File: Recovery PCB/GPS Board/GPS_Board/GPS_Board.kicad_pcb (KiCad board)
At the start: 2 copper layers, 85.7 x 50.8 mm, 9 parts, among them J1 XT30-M, J2 XT30-M, U1 Teensy4.1, U2 D24V22F5_VoltageRegulator, U3 LD1117v33

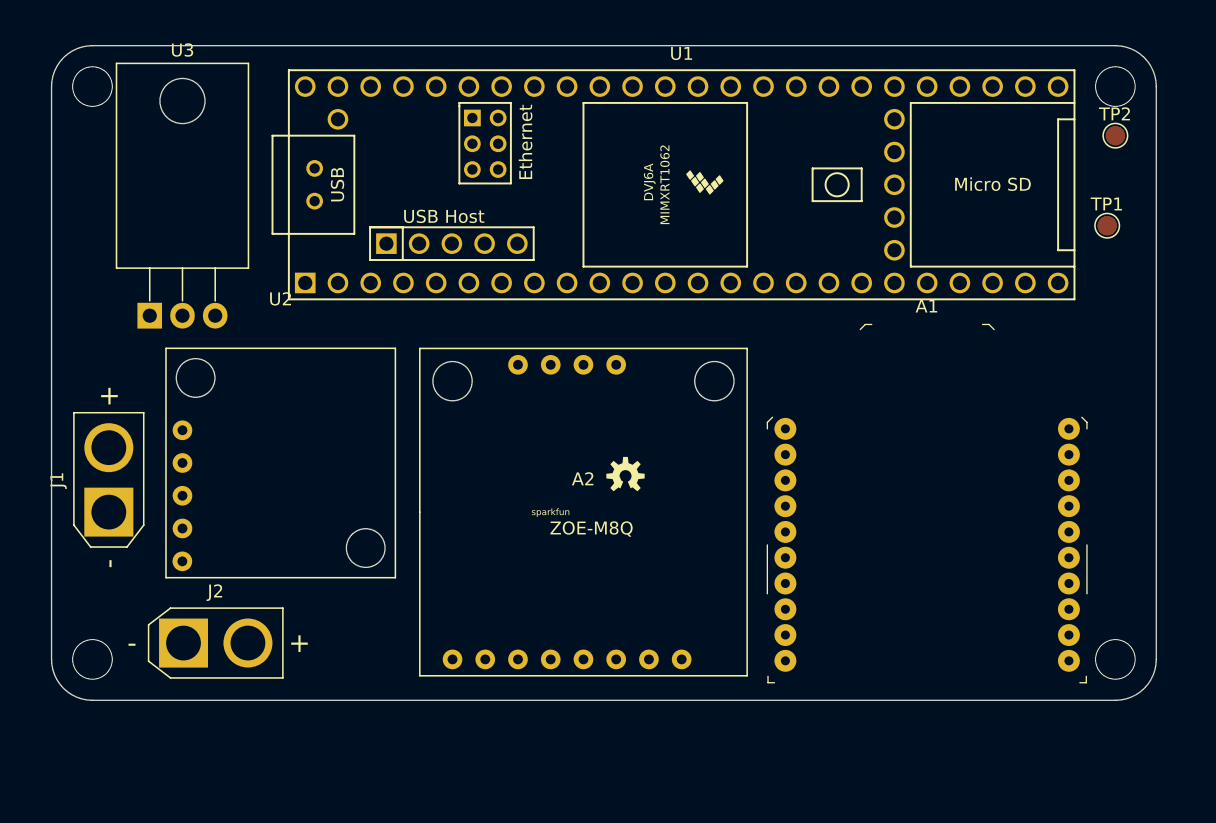
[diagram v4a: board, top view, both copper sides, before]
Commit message: Power Traces Outline
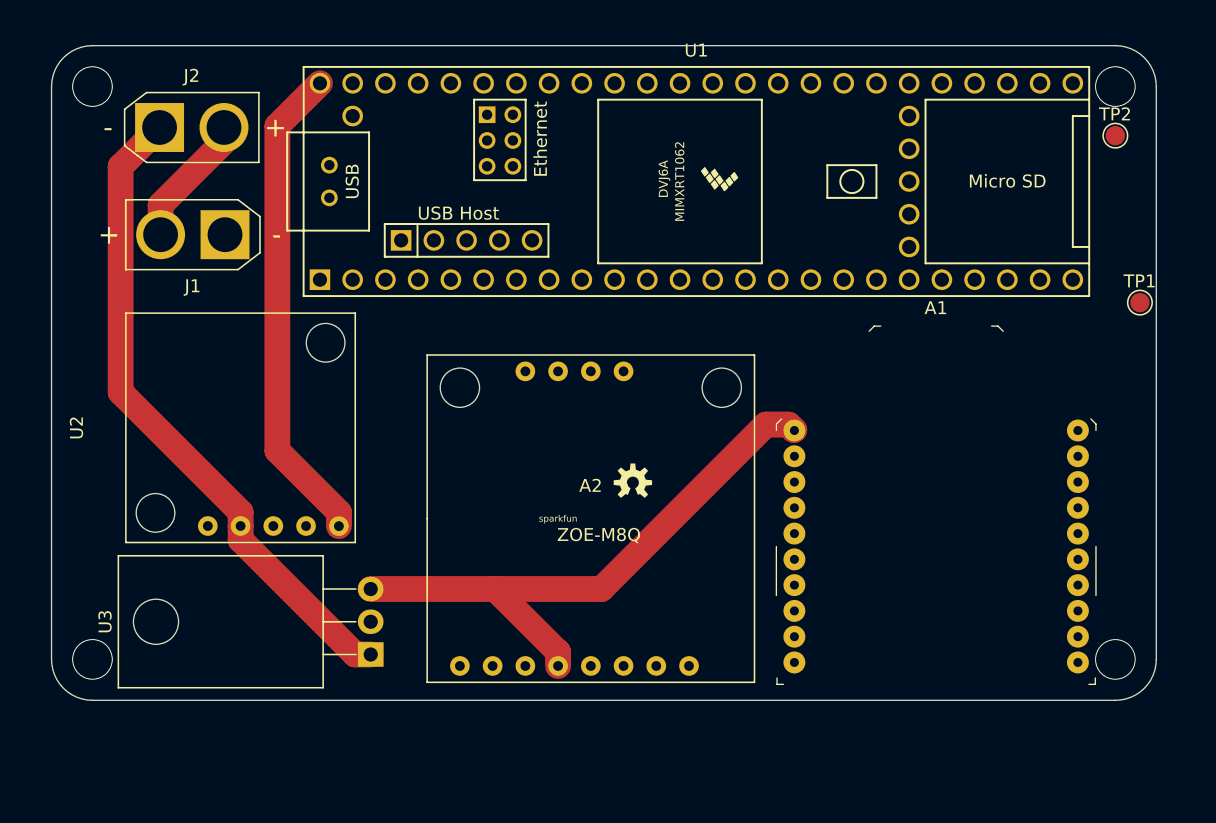
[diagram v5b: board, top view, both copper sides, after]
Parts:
- moved J2 40.0 mm to (119.5, 66.7)
- moved U3 31.4 mm to (135.9, 107.6), turned to 90 degrees
- moved J1 23.3 mm to (124.6, 75.0), turned to 180 degrees
- moved TP1 6.49 mm to (195.6, 80.3)
- moved U2 4.14 mm to (125.8, 90.0), turned to 90 degrees
- moved U1 1.17 mm to (161.2, 70.9)
- moved A2 0.76 mm to (153.0, 97.0)
- moved A1 0.71 mm to (179.8, 99.2)
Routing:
- net Net-(J2-Pad1): track 0.00 -> 50.9 mm
- net +3V3: track 0.00 -> 46.3 mm
- net +5V: track 0.00 -> 37.7 mm
- net Net-(J1-Pad2): track 0.00 -> 10.4 mm
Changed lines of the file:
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@@
     (thickness 1.6)
     (drawings 8)
-    (tracks 4)
+    (tracks 26)
     (zones 0)
     (modules 9)
@@
   )
   (setup
-    (last_trace_width 0.25)
+    (last_trace_width 2)
     (user_trace_width 0.25)
     (user_trace_width 0.4)
@@
   )
   (module "GPS Board:XBEE-20_THT" (layer F.Cu)
-    (at 179.07 99.06)
+    (at 179.7685 99.187)
     (descr https://www.digi.com/pdf/ds_xbeemultipointmodules.pdf)
     (fp_text reference A1 (at 0 -18.49) (layer F.SilkS)
@@
   )
   (module "GPS Board:Sparkfun-GPS-ZOE-M8Q-Breakout" (layer F.Cu)
-    (at 152.4 96.52)
+    (at 152.9715 97.028)
     (fp_text reference A2 (at 0 -2.54) (layer F.SilkS)
       (effects (font (size 1 1) (thickness 0.15)))
@@
   )
   (module Connector_AMASS:AMASS_XT30U-M_1x02_P5.0mm_Vertical (layer F.Cu)
-    (at 115.57 96.52 90)
+    (at 124.587 74.9935 180)
     (descr "Connector XT30 Vertical Cable Male, https://www.tme.eu/en/Document/3cbfa5cfa544d79584972dd5234a409e/XT30U%20SPEC.pdf")
     (tags "RC Connector XT30")
-    (fp_text reference J1 (at 2.5 -4 90) (layer F.SilkS)
-      (effects (font (size 1 1) (thickness 0.15)))
-    )
-    (fp_text value XT30-M (at 2.5 4 90) (layer F.Fab)
+    (fp_text reference J1 (at 2.5 -4) (layer F.SilkS)
+      (effects (font (size 1 1) (thickness 0.15)))
+    )
+    (fp_text value XT30-M (at 2.5 4) (layer F.Fab)
       (effects (font (size 1 1) (thickness 0.15)))
     )
@@
     (fp_line (start 7.6 -2.6) (end 7.6 2.6) (layer F.Fab) (width 0.1))
     (fp_line (start -2.6 -1.3) (end -2.6 1.3) (layer F.Fab) (width 0.1))
-    (fp_text user %R (at 2.5 0 90) (layer F.Fab)
-      (effects (font (size 1 1) (thickness 0.15)))
-    )
-    (fp_text user + (at 9 0 90) (layer F.SilkS)
+    (fp_text user %R (at 2.5 0) (layer F.Fab)
+      (effects (font (size 1 1) (thickness 0.15)))
+    )
+    (fp_text user + (at 9 0) (layer F.SilkS)
       (effects (font (size 1.5 1.5) (thickness 0.15)))
     )
-    (fp_text user - (at -4 0 90) (layer F.SilkS)
+    (fp_text user - (at -4 0) (layer F.SilkS)
       (effects (font (size 1.5 1.5) (thickness 0.15)))
     )
-    (pad 1 thru_hole rect (at 0 0 90) (size 3.8 3.8) (drill 2.7) (layers *.Cu *.Mask)
-      (net 1 GND))
-    (pad 2 thru_hole circle (at 5 0 90) (size 3.8 3.8) (drill 2.7) (layers *.Cu *.Mask)
+    (pad 1 thru_hole rect (at 0 0 180) (size 3.8 3.8) (drill 2.7) (layers *.Cu *.Mask)
+      (net 1 GND))
+    (pad 2 thru_hole circle (at 5 0 180) (size 3.8 3.8) (drill 2.7) (layers *.Cu *.Mask)
       (net 3 "Net-(J1-Pad2)"))
     (model ${KISYS3DMOD}/Connector_AMASS.3dshapes/AMASS_XT30U-M_1x02_P5.0mm_Vertical.wrl
@@
   )
   (module Connector_AMASS:AMASS_XT30U-M_1x02_P5.0mm_Vertical (layer F.Cu)
-    (at 121.365 106.68)
+    (at 119.507 66.675)
     (descr "Connector XT30 Vertical Cable Male, https://www.tme.eu/en/Document/3cbfa5cfa544d79584972dd5234a409e/XT30U%20SPEC.pdf")
     (tags "RC Connector XT30")
@@
   )
   (module TestPoint:TestPoint_Pad_D1.5mm (layer F.Cu)
-    (at 193.04 74.295)
+    (at 195.58 80.264)
     (descr "SMD pad as test Point, diameter 1.5mm")
     (tags "test point SMD pad")
@@
   )
   (module "GPS Board:Teensy41" (layer F.Cu)
-    (at 160.02 71.12)
+    (at 161.163 70.866)
     (fp_text reference U1 (at 0 -10.16) (layer F.SilkS)
       (effects (font (size 1 1) (thickness 0.15)))
@@
   )
   (module "GPS Board:D24V22F5_VoltageRegulator" (layer F.Cu)
-    (at 128.905 92.71)
-    (fp_text reference U2 (at 0 -12.7) (layer F.SilkS)
-      (effects (font (size 1 1) (thickness 0.15)))
-    )
-    (fp_text value D24V22F5_VoltageRegulator (at 0 12.7) (layer F.Fab)
+    (at 125.7935 89.9795 90)
+    (fp_text reference U2 (at 0 -12.7 90) (layer F.SilkS)
+      (effects (font (size 1 1) (thickness 0.15)))
+    )
+    (fp_text value D24V22F5_VoltageRegulator (at 0 12.7 90) (layer F.Fab)
       (effects (font (size 1 1) (thickness 0.15)))
     )
@@
     (fp_line (start 9.3 -9.3) (end -9.3 -9.3) (layer F.CrtYd) (width 0.12))
     (fp_line (start -9.3 -9.3) (end -9.3 -8.8) (layer F.CrtYd) (width 0.12))
-    (pad "" np_thru_hole circle (at -6.6 -6.6) (size 3 3) (drill 3) (layers *.Cu *.Mask))
-    (pad 1 thru_hole circle (at -7.62 -2.54 90) (size 1.524 1.524) (drill 0.762) (layers *.Cu *.Mask)
+    (pad "" np_thru_hole circle (at -6.6 -6.6 90) (size 3 3) (drill 3) (layers *.Cu *.Mask))
+    (pad 1 thru_hole circle (at -7.62 -2.54 180) (size 1.524 1.524) (drill 0.762) (layers *.Cu *.Mask)
       (net 71 "Net-(U2-Pad1)"))
-    (pad 2 thru_hole circle (at -7.62 0) (size 1.524 1.524) (drill 0.762) (layers *.Cu *.Mask)
+    (pad 2 thru_hole circle (at -7.62 0 90) (size 1.524 1.524) (drill 0.762) (layers *.Cu *.Mask)
       (net 34 "Net-(J2-Pad1)"))
-    (pad 5 thru_hole circle (at -7.63 7.63) (size 1.524 1.524) (drill 0.762) (layers *.Cu *.Mask)
+    (pad 5 thru_hole circle (at -7.63 7.63 90) (size 1.524 1.524) (drill 0.762) (layers *.Cu *.Mask)
       (net 2 +5V))
-    (pad 4 thru_hole circle (at -7.62 5.08 90) (size 1.524 1.524) (drill 0.762) (layers *.Cu *.Mask)
-      (net 1 GND))
-    (pad 3 thru_hole circle (at -7.62 2.54) (size 1.524 1.524) (drill 0.762) (layers *.Cu *.Mask)
-      (net 1 GND))
-    (pad "" np_thru_hole circle (at 6.6 6.6) (size 3 3) (drill 3) (layers *.Cu *.Mask))
+    (pad 4 thru_hole circle (at -7.62 5.08 180) (size 1.524 1.524) (drill 0.762) (layers *.Cu *.Mask)
+      (net 1 GND))
+    (pad 3 thru_hole circle (at -7.62 2.54 90) (size 1.524 1.524) (drill 0.762) (layers *.Cu *.Mask)
+      (net 1 GND))
+    (pad "" np_thru_hole circle (at 6.6 6.6 90) (size 3 3) (drill 3) (layers *.Cu *.Mask))
     (model ${KIPRJMOD}/Models/d24v22fx-step-down-voltage-regulator.step
       (offset (xyz -8.85 -8.85 2.75))
@@
   )
   (module Package_TO_SOT_THT:TO-220-3_Horizontal_TabDown (layer F.Cu)
-    (at 118.745 81.28)
+    (at 135.89 107.569 90)
     (descr "TO-220-3, Horizontal, RM 2.54mm, see https://www.vishay.com/docs/66542/to-220-1.pdf")
     (tags "TO-220-3 Horizontal RM 2.54mm")
-    (fp_text reference U3 (at 2.54 -20.58) (layer F.SilkS)
-      (effects (font (size 1 1) (thickness 0.15)))
-    )
-    (fp_text value LD1117v33 (at 2.54 2) (layer F.Fab)
+    (fp_text reference U3 (at 2.54 -20.58 90) (layer F.SilkS)
+      (effects (font (size 1 1) (thickness 0.15)))
+    )
+    (fp_text value LD1117v33 (at 2.54 2 90) (layer F.Fab)
       (effects (font (size 1 1) (thickness 0.15)))
     )
@@
     (fp_line (start -2.46 -13.06) (end -2.46 -19.46) (layer F.Fab) (width 0.1))
     (fp_circle (center 2.54 -16.66) (end 4.39 -16.66) (layer F.Fab) (width 0.1))
-    (fp_text user %R (at 2.54 -20.58) (layer F.Fab)
-      (effects (font (size 1 1) (thickness 0.15)))
-    )
-    (pad "" np_thru_hole oval (at 2.54 -16.66) (size 3.5 3.5) (drill 3.5) (layers *.Cu *.Mask))
-    (pad 1 thru_hole rect (at 0 0) (size 1.905 2) (drill 1.1) (layers *.Cu *.Mask)
+    (fp_text user %R (at 2.54 -20.58 90) (layer F.Fab)
+      (effects (font (size 1 1) (thickness 0.15)))
+    )
+    (pad "" np_thru_hole oval (at 2.54 -16.66 90) (size 3.5 3.5) (drill 3.5) (layers *.Cu *.Mask))
+    (pad 1 thru_hole rect (at 0 0 90) (size 1.905 2) (drill 1.1) (layers *.Cu *.Mask)
       (net 34 "Net-(J2-Pad1)"))
-    (pad 2 thru_hole oval (at 2.54 0) (size 1.905 2) (drill 1.1) (layers *.Cu *.Mask)
-      (net 1 GND))
-    (pad 3 thru_hole oval (at 5.08 0) (size 1.905 2) (drill 1.1) (layers *.Cu *.Mask)
+    (pad 2 thru_hole oval (at 2.54 0 90) (size 1.905 2) (drill 1.1) (layers *.Cu *.Mask)
+      (net 1 GND))
+    (pad 3 thru_hole oval (at 5.08 0 90) (size 1.905 2) (drill 1.1) (layers *.Cu *.Mask)
       (net 6 +3V3))
     (model ${KISYS3DMOD}/Package_TO_SOT_THT.3dshapes/TO-220-3_Horizontal_TabDown.wrl
@@
   (via (at 114.3 107.95) (size 3.15) (drill 3) (layers F.Cu B.Cu) (net 0))
   (via (at 114.3 63.5) (size 3.15) (drill 3) (layers F.Cu B.Cu) (net 0))
+  (segment (start 133.4235 96.53187) (end 128.651 91.75937) (width 2) (layer F.Cu) (net 2))
+  (segment (start 133.4235 97.6095) (end 133.4235 96.53187) (width 2) (layer F.Cu) (net 2))
+  (segment (start 128.651 66.548) (end 131.953 63.246) (width 2) (layer F.Cu) (net 2))
+  (segment (start 128.651 91.75937) (end 128.651 66.548) (width 2) (layer F.Cu) (net 2))
+  (segment (start 119.587 74.9935) (end 119.587 72.691) (width 2) (layer F.Cu) (net 3))
+  (segment (start 124.507 67.771) (end 124.507 66.675) (width 2) (layer F.Cu) (net 3))
+  (segment (start 119.587 72.691) (end 124.507 67.771) (width 2) (layer F.Cu) (net 3))
+  (segment (start 150.4315 107.38037) (end 150.4315 108.458) (width 2) (layer F.Cu) (net 6))
+  (segment (start 145.54013 102.489) (end 150.4315 107.38037) (width 2) (layer F.Cu) (net 6))
+  (segment (start 135.89 102.489) (end 145.54013 102.489) (width 2) (layer F.Cu) (net 6))
+  (segment (start 145.54013 102.489) (end 153.797 102.489) (width 2) (layer F.Cu) (net 6))
+  (segment (start 168.718499 90.136999) (end 168.7685 90.136999) (width 2) (layer F.Cu) (net 6))
+  (segment (start 166.5605 89.7255) (end 168.307 89.7255) (width 2) (layer F.Cu) (net 6))
+  (segment (start 153.797 102.489) (end 166.5605 89.7255) (width 2) (layer F.Cu) (net 6))
+  (segment (start 168.307 89.7255) (end 168.718499 90.136999) (width 2) (layer F.Cu) (net 6))
+  (segment (start 134.68537 107.569) (end 135.89 107.569) (width 2) (layer F.Cu) (net 34))
+  (segment (start 125.7935 98.67713) (end 134.68537 107.569) (width 2) (layer F.Cu) (net 34))
+  (segment (start 125.7935 97.5995) (end 125.7935 98.67713) (width 2) (layer F.Cu) (net 34))
+  (segment (start 125.7935 96.52187) (end 125.7935 97.5995) (width 2) (layer F.Cu) (net 34))
+  (segment (start 116.486999 69.695001) (end 116.486999 87.215369) (width 2) (layer F.Cu) (net 34))
+  (segment (start 116.486999 87.215369) (end 125.7935 96.52187) (width 2) (layer F.Cu) (net 34))
+  (segment (start 119.507 66.675) (end 116.486999 69.695001) (width 2) (layer F.Cu) (net 34))
 )

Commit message: Did row of traces from Teensy
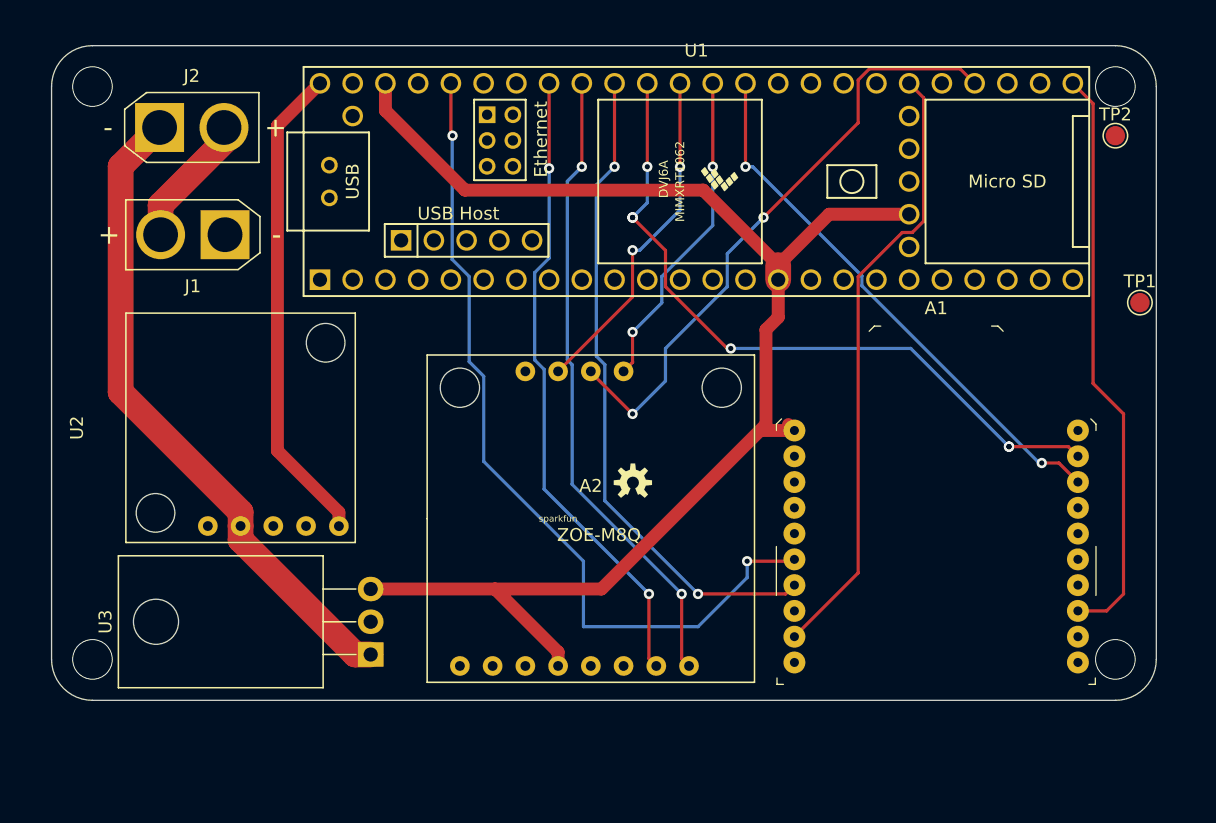
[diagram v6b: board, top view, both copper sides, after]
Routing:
- net /XBee_PWM: track 0.00 -> 65.7 mm, vias 0 -> 2
- net +3V3: track 46.3 -> 109.1 mm
- net /XBEE_SCL: track 0.00 -> 54.8 mm, vias 0 -> 7
- net /XBEE_SDA: track 0.00 -> 51.2 mm, vias 0 -> 2
- net /GPS_SDA: track 0.00 -> 49.6 mm, vias 0 -> 2
- net /GPS_SCL: track 0.00 -> 49.6 mm, vias 0 -> 2
- net /XBee_DTR: track 0.00 -> 48.0 mm
- net /GPS_RESET: track 0.00 -> 47.7 mm, vias 0 -> 2
- net /XBEE_SLEEP: track 0.00 -> 45.3 mm
- net /XBee_SCK: track 0.00 -> 42.9 mm, vias 0 -> 2
- net /GPS_PPS: track 0.00 -> 26.6 mm, vias 0 -> 2
- net /GPS_INT: track 0.00 -> 25.2 mm, vias 0 -> 2

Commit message: bris changes
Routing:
- net /XBee_MISO: track 0.00 -> 27.5 mm, vias 0 -> 3
- net /XBEE_RX: track 0.00 -> 21.5 mm, vias 0 -> 2
- net /XBEE_TX: track 0.00 -> 18.4 mm, vias 0 -> 3
- net /XBee_MOSI: track 0.00 -> 4.64 mm
- net /XBee_DTR: track 48.0 -> 49.6 mm

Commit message: Finished More Traces
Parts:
- moved A1 0.71 mm to (179.1, 99.1), turned to 180 degrees
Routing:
- net /XBee_MISO: track 27.5 -> 180.8 mm, vias 3 -> 2
- net +3V3: track 109.1 -> 149.7 mm
- net /GPS_TX: track 0.00 -> 36.0 mm, vias 0 -> 2
- net /GPS_RX: track 0.00 -> 35.3 mm, vias 0 -> 2
- net /XBee_CS: track 0.00 -> 30.9 mm, vias 0 -> 2
- net /XBEE_SDA: track 51.2 -> 78.9 mm, vias 2 -> 0
- net /GPS_INT: track 25.2 -> 47.6 mm, vias 2 -> 4
- net /XBee_PWM: track 65.7 -> 87.5 mm, vias 2 -> 0
- net /XBEE_TX: track 18.4 -> 34.7 mm, vias 3 -> 0
- net /XBee_MOSI: track 4.64 -> 17.5 mm, vias 0 -> 2
- net /XBee_SCK: track 42.9 -> 54.1 mm, vias 2 -> 4
- net /GPS_RESET: track 47.7 -> 58.6 mm, vias 2 -> 4
- net /XBEE_RX: track 21.5 -> 32.1 mm, vias 2 -> 0
- net /XBee_DTR: track 49.6 -> 39.0 mm
- net /XBEE_SCL: track 54.8 -> 51.5 mm, vias 7 -> 4
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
